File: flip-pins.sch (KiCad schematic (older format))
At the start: 3 parts, among them J1 FLIP-PINS-08, J2 FLIP-PINS-14, J3 FLIP-PINS-20

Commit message: added images
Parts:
- J1: footprint (none) -> flip-pins:FLIP-PINS-08
- J2: footprint (none) -> flip-pins:FLIP-PINS-14
- J3: footprint (none) -> flip-pins:FLIP-PINS-20
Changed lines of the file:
@@
 EESchema Schematic File Version 2
-LIBS:osh_chip
+LIBS:flip-pins
 LIBS:power
-LIBS:oshchip-cache
+LIBS:flip-pins-cache
 EELAYER 25 0
 EELAYER END
@@
 F 0 "J1" H 2900 3525 40  0000 L CNB
 F 1 "FLIP-PINS-08" H 2900 3450 40  0000 L CNB
-F 2 "" H 3000 3000 60  0000 C CNN
+F 2 "flip-pins:FLIP-PINS-08" H 3000 3000 60  0001 C CNN
 F 3 "" H 3000 3000 60  0000 C CNN
 	1    3000 3000
@@
 F 0 "J2" H 3900 3825 40  0000 L CNB
 F 1 "FLIP-PINS-14" H 3900 3750 40  0000 L CNB
-F 2 "" H 4000 3300 60  0000 C CNN
+F 2 "flip-pins:FLIP-PINS-14" H 4000 3300 60  0001 C CNN
 F 3 "" H 4000 3300 60  0000 C CNN
 F 4 "mfr_pn" H 4000 3000 60  0001 C CNN "manf#"
@@
 F 0 "J3" H 4900 4125 40  0000 L CNB
 F 1 "FLIP-PINS-20" H 4900 4050 40  0000 L CNB
-F 2 "" H 5000 3600 60  0000 C CNN
+F 2 "flip-pins:FLIP-PINS-20" H 5000 3600 60  0001 C CNN
 F 3 "" H 5000 3600 60  0000 C CNN
 F 4 "mfr_pn" H 5000 3300 60  0001 C CNN "manf#"

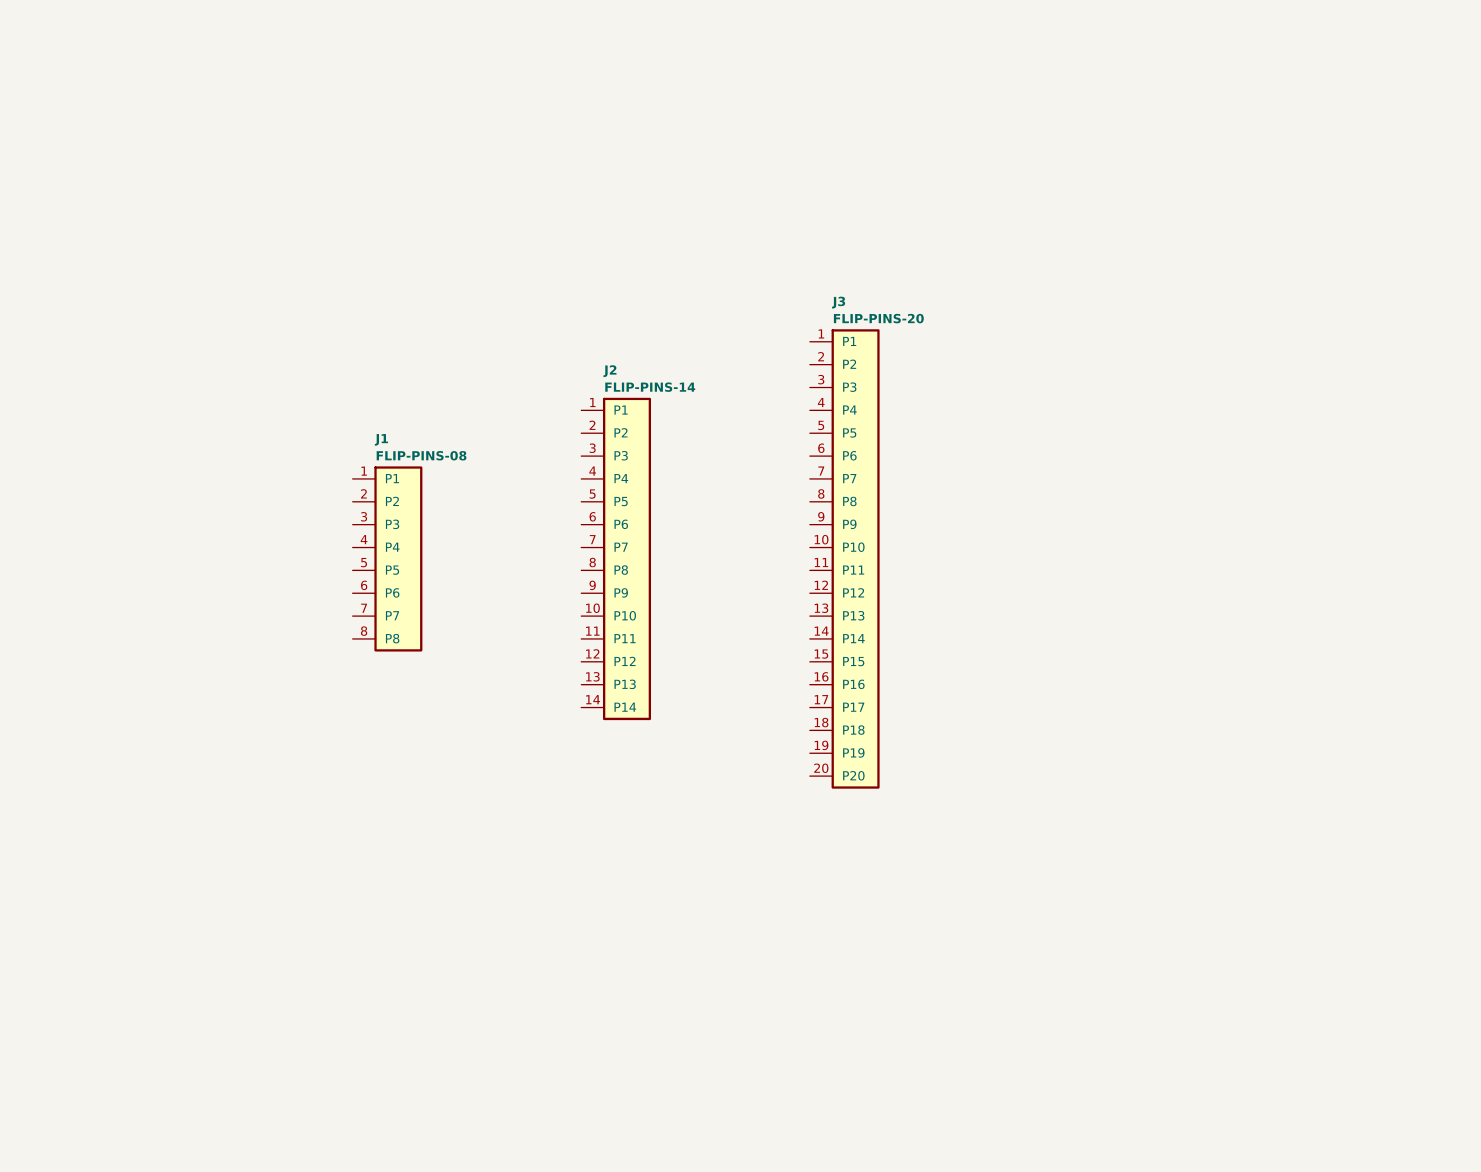
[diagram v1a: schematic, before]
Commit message: added separate schematic, footprint, 3D versions of floating and aligner pins
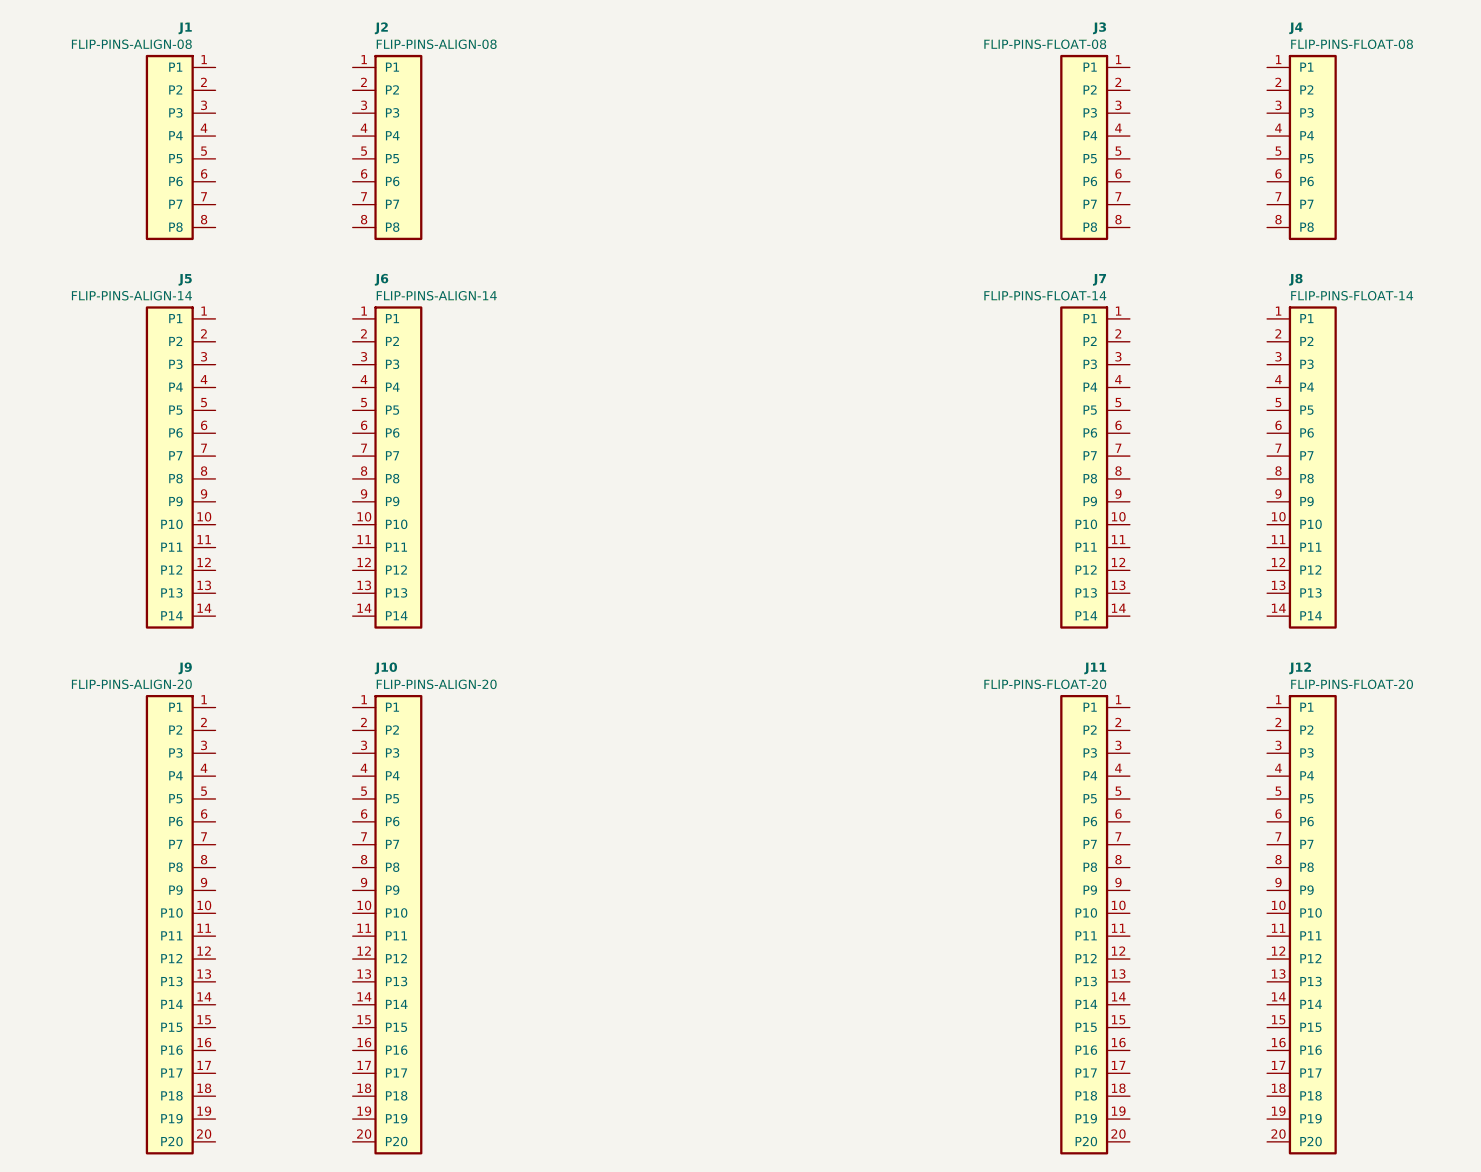
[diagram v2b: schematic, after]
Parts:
- removed J1: FLIP-PINS-08, flip-pins:FLIP-PINS-08, symbol FLIP-PINS-08
- removed J2: FLIP-PINS-14, flip-pins:FLIP-PINS-14, symbol FLIP-PINS-14
- removed J3: FLIP-PINS-20, flip-pins:FLIP-PINS-20, symbol FLIP-PINS-20
- added J1, J2: FLIP-PINS-ALIGN-08, flip-pins:FLIP-PINS-ALIGN-08, symbol FLIP-PINS-ALIGN-08
- added J10, J9: FLIP-PINS-ALIGN-20, flip-pins:FLIP-PINS-ALIGN-20, symbol FLIP-PINS-ALIGN-20
- added J11, J12: FLIP-PINS-FLOAT-20, flip-pins:FLIP-PINS-FLOAT-20, symbol FLIP-PINS-FLOAT-20
- added J3, J4: FLIP-PINS-FLOAT-08, flip-pins:FLIP-PINS-FLOAT-08, symbol FLIP-PINS-FLOAT-08
- added J5, J6: FLIP-PINS-ALIGN-14, flip-pins:FLIP-PINS-ALIGN-14, symbol FLIP-PINS-ALIGN-14
- added J7, J8: FLIP-PINS-FLOAT-14, flip-pins:FLIP-PINS-FLOAT-14, symbol FLIP-PINS-FLOAT-14
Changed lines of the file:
@@
 $EndDescr
 $Comp
-L FLIP-PINS-08 J1
-U 1 1 57D434DA
-P 3000 3000
-F 0 "J1" H 2900 3525 40  0000 L CNB
-F 1 "FLIP-PINS-08" H 2900 3450 40  0000 L CNB
-F 2 "flip-pins:FLIP-PINS-08" H 3000 3000 60  0001 C CNN
-F 3 "" H 3000 3000 60  0000 C CNN
-	1    3000 3000
+L FLIP-PINS-ALIGN-08 J2
+U 1 1 57D6974D
+P 3000 1200
+F 0 "J2" H 2900 1725 40  0000 L CNB
+F 1 "FLIP-PINS-ALIGN-08" H 2900 1650 40  0000 L CNN
+F 2 "flip-pins:FLIP-PINS-ALIGN-08" H 3000 1200 60  0001 C CNN
+F 3 "" H 3000 1200 60  0000 C CNN
+	1    3000 1200
 	1    0    0    -1
 $EndComp
 $Comp
-L FLIP-PINS-14 J2
-U 1 1 57D435E4
-P 4000 3000
-F 0 "J2" H 3900 3825 40  0000 L CNB
-F 1 "FLIP-PINS-14" H 3900 3750 40  0000 L CNB
-F 2 "flip-pins:FLIP-PINS-14" H 4000 3300 60  0001 C CNN
-F 3 "" H 4000 3300 60  0000 C CNN
-F 4 "mfr_pn" H 4000 3000 60  0001 C CNN "manf#"
-	1    4000 3000
+L FLIP-PINS-ALIGN-14 J6
+U 1 1 57D69803
+P 3000 2600
+F 0 "J6" H 2900 3425 40  0000 L CNB
+F 1 "FLIP-PINS-ALIGN-14" H 2900 3350 40  0000 L CNN
+F 2 "flip-pins:FLIP-PINS-ALIGN-14" H 3000 2900 60  0001 C CNN
+F 3 "" H 3000 2900 60  0000 C CNN
+F 4 "mfr_pn" H 3000 2600 60  0001 C CNN "manf#"
+	1    3000 2600
 	1    0    0    -1
 $EndComp
 $Comp
-L FLIP-PINS-20 J3
-U 1 1 57D43647
-P 5000 3000
-F 0 "J3" H 4900 4125 40  0000 L CNB
-F 1 "FLIP-PINS-20" H 4900 4050 40  0000 L CNB
-F 2 "flip-pins:FLIP-PINS-20" H 5000 3600 60  0001 C CNN
-F 3 "" H 5000 3600 60  0000 C CNN
-F 4 "mfr_pn" H 5000 3300 60  0001 C CNN "manf#"
-	1    5000 3000
+L FLIP-PINS-ALIGN-20 J10
+U 1 1 57D698AA
+P 3000 4600
+F 0 "J10" H 2900 5725 40  0000 L CNB
+F 1 "FLIP-PINS-ALIGN-20" H 2900 5650 40  0000 L CNN
+F 2 "flip-pins:FLIP-PINS-ALIGN-20" H 3000 5200 60  0001 C CNN
+F 3 "" H 3000 5200 60  0000 C CNN
+F 4 "mfr_pn" H 3000 4900 60  0001 C CNN "manf#"
+	1    3000 4600
 	1    0    0    -1
 $EndComp
+$Comp
+L FLIP-PINS-FLOAT-08 J4
+U 1 1 57D69981
+P 7000 1200
+F 0 "J4" H 6900 1725 40  0000 L CNB
+F 1 "FLIP-PINS-FLOAT-08" H 6900 1650 40  0000 L CNN
+F 2 "flip-pins:FLIP-PINS-FLOAT-08" H 7000 1200 60  0001 C CNN
+F 3 "" H 7000 1200 60  0000 C CNN
+F 4 "Value" H 7000 1200 60  0001 C CNN "manf#"
+	1    7000 1200
+	1    0    0    -1
+$EndComp
+$Comp
+L FLIP-PINS-FLOAT-14 J8
+U 1 1 57D699AE
+P 7000 2600
+F 0 "J8" H 6900 3425 40  0000 L CNB
+F 1 "FLIP-PINS-FLOAT-14" H 6900 3350 40  0000 L CNN
+F 2 "flip-pins:FLIP-PINS-FLOAT-14" H 7000 2900 60  0001 C CNN
+F 3 "" H 7000 2900 60  0000 C CNN
+F 4 "mfr_pn" H 7000 2600 60  0001 C CNN "manf#"
+	1    7000 2600
+	1    0    0    -1
+$EndComp
+$Comp
+L FLIP-PINS-FLOAT-20 J12
+U 1 1 57D699E3
+P 7000 4600
+F 0 "J12" H 6900 5725 40  0000 L CNB
+F 1 "FLIP-PINS-FLOAT-20" H 6900 5650 40  0000 L CNN
+F 2 "flip-pins:FLIP-PINS-FLOAT-20" H 7000 5200 60  0001 C CNN
+F 3 "" H 7000 5200 60  0000 C CNN
+F 4 "mfr_pn" H 7000 4900 60  0001 C CNN "manf#"
+	1    7000 4600
+	1    0    0    -1
+$EndComp
+$Comp
+L FLIP-PINS-ALIGN-08 J1
+U 1 1 57D6AD18
+P 2000 1200
+F 0 "J1" H 1900 1725 40  0000 L CNB
+F 1 "FLIP-PINS-ALIGN-08" H 1900 1650 40  0000 L CNN
+F 2 "flip-pins:FLIP-PINS-ALIGN-08" H 2000 1200 60  0001 C CNN
+F 3 "" H 2000 1200 60  0000 C CNN
+	1    2000 1200
+	-1   0    0    -1
+$EndComp
+$Comp
+L FLIP-PINS-ALIGN-14 J5
+U 1 1 57D6AD1F
+P 2000 2600
+F 0 "J5" H 1900 3425 40  0000 L CNB
+F 1 "FLIP-PINS-ALIGN-14" H 1900 3350 40  0000 L CNN
+F 2 "flip-pins:FLIP-PINS-ALIGN-14" H 2000 2900 60  0001 C CNN
+F 3 "" H 2000 2900 60  0000 C CNN
+F 4 "mfr_pn" H 2000 2600 60  0001 C CNN "manf#"
+	1    2000 2600
+	-1   0    0    -1
+$EndComp
+$Comp
+L FLIP-PINS-ALIGN-20 J9
+U 1 1 57D6AD26
+P 2000 4600
+F 0 "J9" H 1900 5725 40  0000 L CNB
+F 1 "FLIP-PINS-ALIGN-20" H 1900 5650 40  0000 L CNN
+F 2 "flip-pins:FLIP-PINS-ALIGN-20" H 2000 5200 60  0001 C CNN
+F 3 "" H 2000 5200 60  0000 C CNN
+F 4 "mfr_pn" H 2000 4900 60  0001 C CNN "manf#"
+	1    2000 4600
+	-1   0    0    -1
+$EndComp
+$Comp
+L FLIP-PINS-FLOAT-08 J3
+U 1 1 57D6AD2D
+P 6000 1200
+F 0 "J3" H 5900 1725 40  0000 L CNB
+F 1 "FLIP-PINS-FLOAT-08" H 5900 1650 40  0000 L CNN
+F 2 "flip-pins:FLIP-PINS-FLOAT-08" H 6000 1200 60  0001 C CNN
+F 3 "" H 6000 1200 60  0000 C CNN
+F 4 "Value" H 6000 1200 60  0001 C CNN "manf#"
+	1    6000 1200
+	-1   0    0    -1
+$EndComp
+$Comp
+L FLIP-PINS-FLOAT-14 J7
+U 1 1 57D6AD34
+P 6000 2600
+F 0 "J7" H 5900 3425 40  0000 L CNB
+F 1 "FLIP-PINS-FLOAT-14" H 5900 3350 40  0000 L CNN
+F 2 "flip-pins:FLIP-PINS-FLOAT-14" H 6000 2900 60  0001 C CNN
+F 3 "" H 6000 2900 60  0000 C CNN
+F 4 "mfr_pn" H 6000 2600 60  0001 C CNN "manf#"
+	1    6000 2600
+	-1   0    0    -1
+$EndComp
+$Comp
+L FLIP-PINS-FLOAT-20 J11
+U 1 1 57D6AD3B
+P 6000 4600
+F 0 "J11" H 5900 5725 40  0000 L CNB
+F 1 "FLIP-PINS-FLOAT-20" H 5900 5650 40  0000 L CNN
+F 2 "flip-pins:FLIP-PINS-FLOAT-20" H 6000 5200 60  0001 C CNN
+F 3 "" H 6000 5200 60  0000 C CNN
+F 4 "mfr_pn" H 6000 4900 60  0001 C CNN "manf#"
+	1    6000 4600
+	-1   0    0    -1
+$EndComp
 $EndSCHEMATC
